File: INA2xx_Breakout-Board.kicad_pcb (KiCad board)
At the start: 2 copper layers, 20.3 x 15.2 mm, 4 parts, among them J1 Conn_01x05_Male, J2 Conn_01x05_Male, U1 INA226

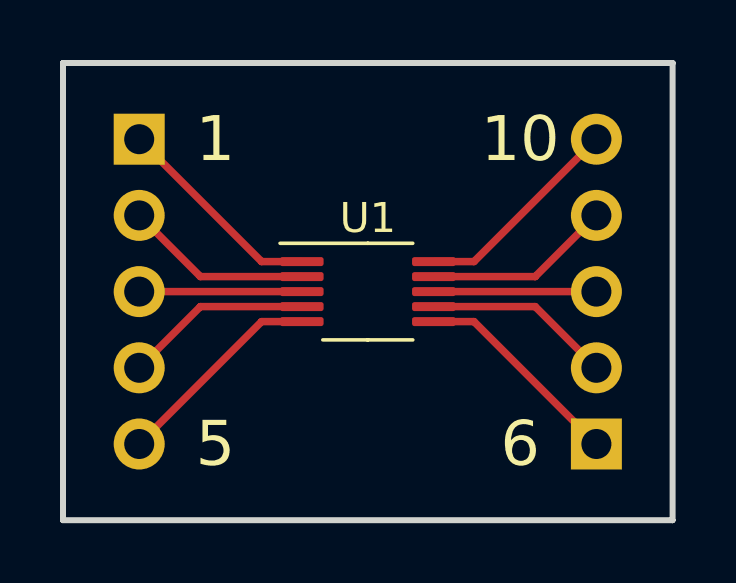
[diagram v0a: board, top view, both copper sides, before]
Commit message: Mod: Updated the project name and revision to be on the copper layer now
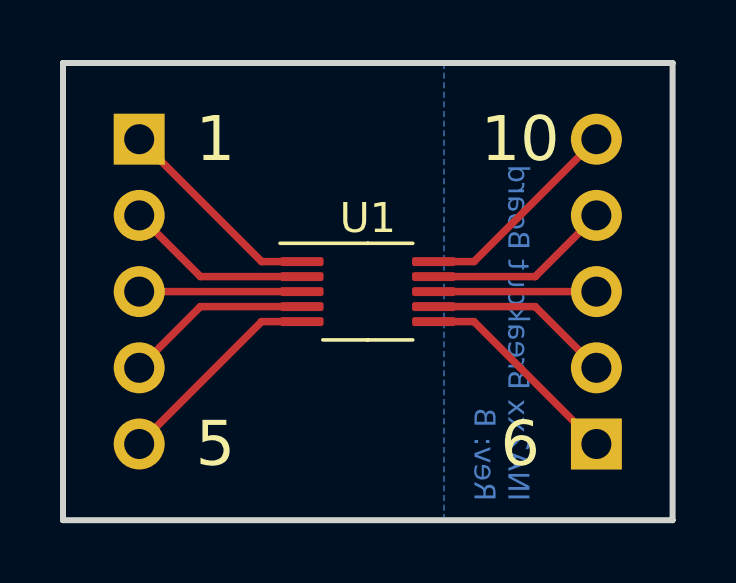
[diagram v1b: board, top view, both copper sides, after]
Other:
- board text added: "${TITLE} Rev: ${REVISION}"
- board text removed: "Prj: ${TITLE} Rev: ${REVISION}"
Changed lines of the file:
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@@
   (title_block
     (title "INA2xx Breakout Board")
-    (date "2023-03-06")
-    (rev "A")
+    (date "2023-03-07")
+    (rev "B")
     (company "ElektroNik Zoller")
-    (comment 1 "Author: Nikolai Zoller")
-    (comment 4 "License: CERN-OHL-P")
+    (comment 1 "Nikolai Zoller")
+    (comment 4 "CERN-OHL-P")
   )
   (layers
@@
     (property "Sheetname" "")
     (attr through_hole)
-    (fp_text reference "J2" (at -2.54 0 180) (layer "B.SilkS")
+    (fp_text reference "J2" (at -2.54 -11.43 180) (layer "B.SilkS")
       (effects (font (size 1 1) (thickness 0.15)) (justify mirror))
     )
@@
     (property "Sheetname" "")
     (attr through_hole)
-    (fp_text reference "J1" (at -2.54 0) (layer "B.SilkS")
+    (fp_text reference "J1" (at -2.54 1.27) (layer "B.SilkS")
       (effects (font (size 1 1) (thickness 0.15)) (justify mirror))
     )
@@
   )
   (gr_rect (start 142.24 93.98) (end 162.56 109.22) (layer "Edge.Cuts") (width 0.2) (fill none))
+  (gr_text "${TITLE}\nRev: ${REVISION}" (at 156.845 108.585 270) (layer "B.Cu")
+    (effects (font (size 0.7 0.7) (thickness 0.15)) (justify left mirror))
+  )
   (gr_text "5" (at 147.32 106.68) (layer "F.SilkS")
     (effects (font (size 1.5 1.5) (thickness 0.3)))
@@
   (gr_text "6" (at 157.48 106.68) (layer "F.SilkS")
     (effects (font (size 1.5 1.5) (thickness 0.3)))
-  )
-  (gr_text "Prj: ${TITLE}\nRev: ${REVISION}" (at 152.4 105.41) (layer "B.Mask")
-    (effects (font (size 0.4 0.4) (thickness 0.1)) (justify mirror))
   )
   (segment (start 144.78 96.52) (end 148.86 100.6) (width 0.25) (layer "F.Cu") (net 1))
@@
     (polygon
       (pts
-        (xy 162.56 109.22)
+        (xy 154.94 109.22)
         (xy 142.24 109.22)
         (xy 142.24 93.98)
-        (xy 162.56 93.98)
+        (xy 154.94 93.98)
       )
     )
